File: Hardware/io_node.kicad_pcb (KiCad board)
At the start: 2 copper layers, 60 x 90 mm, 135 parts, among them J1 Conn_01x09, J10 Conn_01x04, J2 Conn_01x09, J3 Conn_01x09, J4 Conn_01x05, J5 USB_B_Micro, J6 Conn_01x05, J7 Conn_01x05, J8 Conn_01x02, J9 Conn_01x04, Q1 2N7002, Q2 2N7002, Q3 2N7002, Q4 2N7002, Q5 2N7002, Q6 2N7002, Q7 2N7002, Q8 2N7002, U1 STM32F103RBT6, U10 EL357N-G, U11 EL357N-G, U12 EL357N-G, U13 EL357N-G, U14 EL357N-G, U15 USBLC6-2SC6, U2 AMS1117-5.0, U3 AMS1117-3.3, U4 SP3485EN, U5 TLV274CPWR, U6 TLV274CPWR, U7 EL357N-G, U8 EL357N-G, U9 EL357N-G, Y1 8 MHz

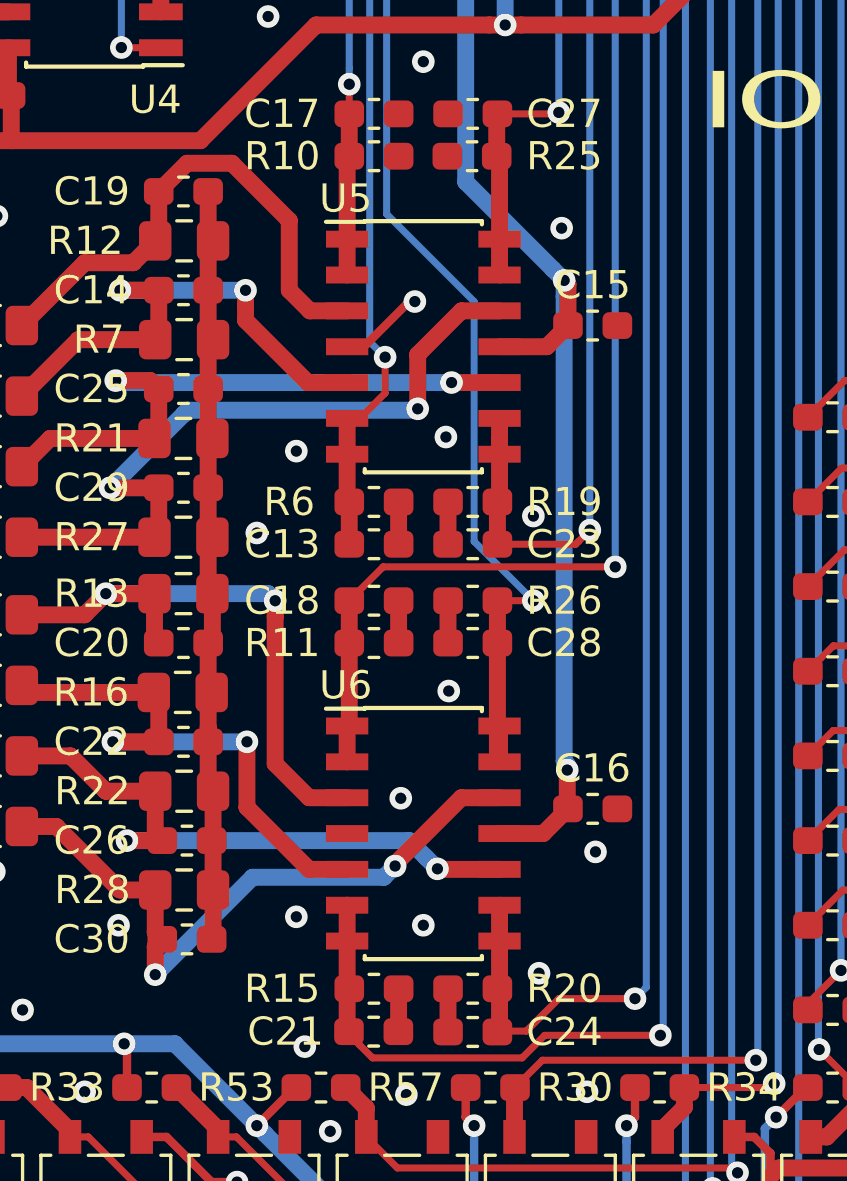
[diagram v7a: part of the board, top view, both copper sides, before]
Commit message: OP-AMP power was incorrect
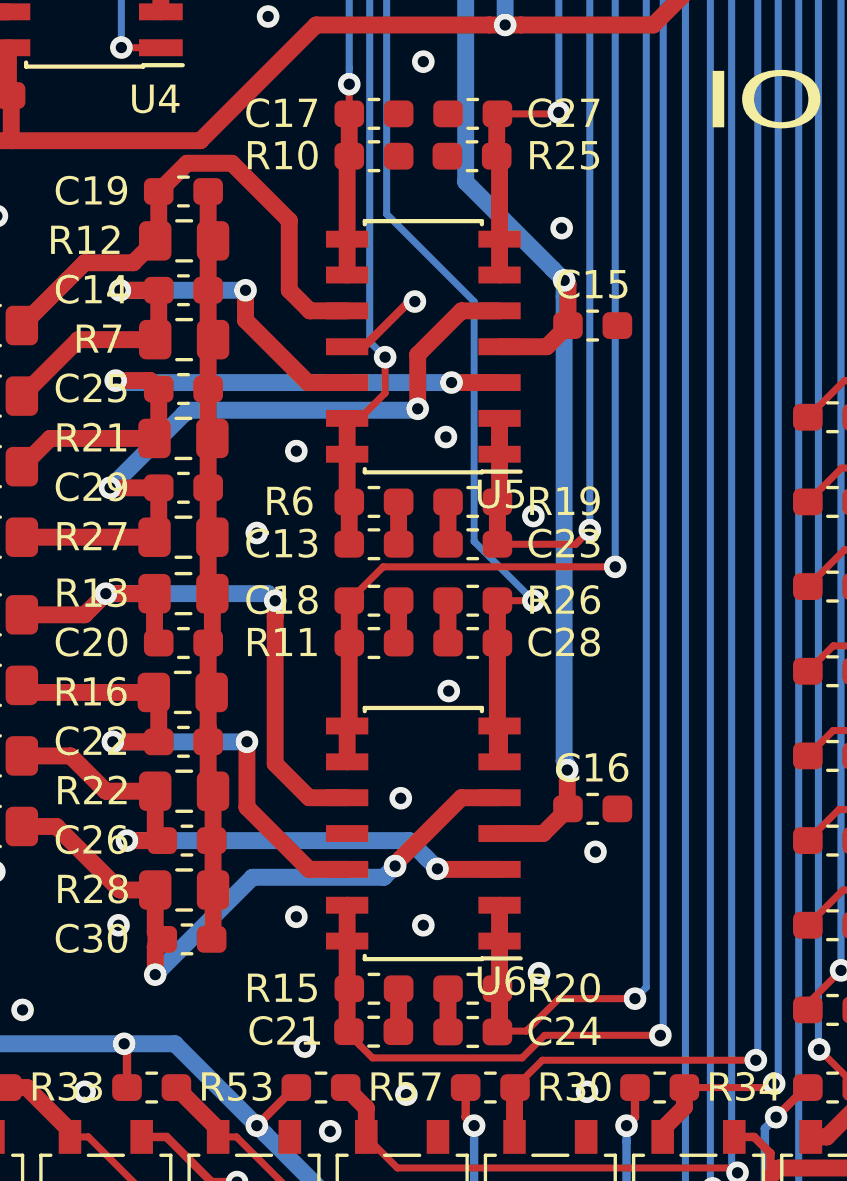
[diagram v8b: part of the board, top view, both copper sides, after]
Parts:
- U5, U6: value TLV274CPWR -> LM324DT
- turned U5 to 180 degrees
- turned U6 to 180 degrees
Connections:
- U5 pad 1: /ADC_IN0 -> /ADC_IN5
- U5 pad 10: Net-(C25-Pad1) -> Net-(C19-Pad1)
- U5 pad 11: +3.3VA -> GND
- U5 pad 12: Net-(C29-Pad1) -> Net-(C14-Pad1)
- U5 pad 13: /ADC_IN6 -> /ADC_IN1
- U5 pad 14: /ADC_IN6 -> /ADC_IN1
- U5 pad 2: /ADC_IN0 -> /ADC_IN5
- U5 pad 3: Net-(C19-Pad1) -> Net-(C25-Pad1)
- U5 pad 4: GND -> +3.3VA
- U5 pad 5: Net-(C14-Pad1) -> Net-(C29-Pad1)
- U5 pad 6: /ADC_IN1 -> /ADC_IN6
- U5 pad 7: /ADC_IN1 -> /ADC_IN6
- U5 pad 8: /ADC_IN5 -> /ADC_IN0
- U5 pad 9: /ADC_IN5 -> /ADC_IN0
- U6 pad 1: /ADC_IN7 -> /ADC_IN9
- U6 pad 10: Net-(C26-Pad1) -> Net-(C20-Pad1)
- U6 pad 11: +3.3VA -> GND
- U6 pad 12: Net-(C30-Pad1) -> Net-(C22-Pad1)
- U6 pad 13: /ADC_IN10 -> /ADC_IN8
- U6 pad 14: /ADC_IN10 -> /ADC_IN8
- U6 pad 2: /ADC_IN7 -> /ADC_IN9
- U6 pad 3: Net-(C20-Pad1) -> Net-(C26-Pad1)
- U6 pad 4: GND -> +3.3VA
- U6 pad 5: Net-(C22-Pad1) -> Net-(C30-Pad1)
- U6 pad 6: /ADC_IN8 -> /ADC_IN10
- U6 pad 7: /ADC_IN8 -> /ADC_IN10
- U6 pad 8: /ADC_IN9 -> /ADC_IN7
- U6 pad 9: /ADC_IN9 -> /ADC_IN7
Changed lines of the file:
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@@
   )
   (module Package_SO:SOIC-14_3.9x8.7mm_P1.27mm (layer F.Cu)
-    (at 69 59)
+    (at 69 59 180)
     (descr "14-Lead Plastic Small Outline (SL) - Narrow, 3.90 mm Body [SOIC] (see Microchip Packaging Specification 00000049BS.pdf)")
     (tags "SOIC 1.27")
     (attr smd)
-    (fp_text reference U5 (at -2.75 -5.25) (layer F.SilkS)
-      (effects (font (size 1 1) (thickness 0.15)))
-    )
-    (fp_text value TLV274CPWR (at 0 5.375) (layer F.Fab)
-      (effects (font (size 1 1) (thickness 0.15)))
-    )
-    (fp_text user %R (at 0 0) (layer F.Fab)
+    (fp_text reference U5 (at -2.75 -5.25 180) (layer F.SilkS)
+      (effects (font (size 1 1) (thickness 0.15)))
+    )
+    (fp_text value LM324DT (at 0 5.375 180) (layer F.Fab)
+      (effects (font (size 1 1) (thickness 0.15)))
+    )
+    (fp_text user %R (at 0 0 180) (layer F.Fab)
       (effects (font (size 0.9 0.9) (thickness 0.135)))
     )
@@
     (fp_line (start -2.075 4.45) (end 2.075 4.45) (layer F.SilkS) (width 0.15))
     (fp_line (start -2.075 -4.425) (end -3.45 -4.425) (layer F.SilkS) (width 0.15))
-    (pad 1 smd rect (at -2.7 -3.81) (size 1.5 0.6) (layers F.Cu F.Paste F.Mask)
+    (pad 1 smd rect (at -2.7 -3.81 180) (size 1.5 0.6) (layers F.Cu F.Paste F.Mask)
+      (net 26 /ADC_IN5))
+    (pad 2 smd rect (at -2.7 -2.54 180) (size 1.5 0.6) (layers F.Cu F.Paste F.Mask)
+      (net 26 /ADC_IN5))
+    (pad 3 smd rect (at -2.7 -1.27 180) (size 1.5 0.6) (layers F.Cu F.Paste F.Mask)
+      (net 35 "Net-(C25-Pad1)"))
+    (pad 4 smd rect (at -2.7 0 180) (size 1.5 0.6) (layers F.Cu F.Paste F.Mask)
+      (net 14 +3.3VA))
+    (pad 5 smd rect (at -2.7 1.27 180) (size 1.5 0.6) (layers F.Cu F.Paste F.Mask)
+      (net 37 "Net-(C29-Pad1)"))
+    (pad 6 smd rect (at -2.7 2.54 180) (size 1.5 0.6) (layers F.Cu F.Paste F.Mask)
+      (net 27 /ADC_IN6))
+    (pad 7 smd rect (at -2.7 3.81 180) (size 1.5 0.6) (layers F.Cu F.Paste F.Mask)
+      (net 27 /ADC_IN6))
+    (pad 8 smd rect (at 2.7 3.81 180) (size 1.5 0.6) (layers F.Cu F.Paste F.Mask)
       (net 24 /ADC_IN0))
-    (pad 2 smd rect (at -2.7 -2.54) (size 1.5 0.6) (layers F.Cu F.Paste F.Mask)
+    (pad 9 smd rect (at 2.7 2.54 180) (size 1.5 0.6) (layers F.Cu F.Paste F.Mask)
       (net 24 /ADC_IN0))
-    (pad 3 smd rect (at -2.7 -1.27) (size 1.5 0.6) (layers F.Cu F.Paste F.Mask)
+    (pad 10 smd rect (at 2.7 1.27 180) (size 1.5 0.6) (layers F.Cu F.Paste F.Mask)
       (net 32 "Net-(C19-Pad1)"))
-    (pad 4 smd rect (at -2.7 0) (size 1.5 0.6) (layers F.Cu F.Paste F.Mask)
-      (net 1 GND))
-    (pad 5 smd rect (at -2.7 1.27) (size 1.5 0.6) (layers F.Cu F.Paste F.Mask)
+    (pad 11 smd rect (at 2.7 0 180) (size 1.5 0.6) (layers F.Cu F.Paste F.Mask)
+      (net 1 GND))
+    (pad 12 smd rect (at 2.7 -1.27 180) (size 1.5 0.6) (layers F.Cu F.Paste F.Mask)
       (net 31 "Net-(C14-Pad1)"))
-    (pad 6 smd rect (at -2.7 2.54) (size 1.5 0.6) (layers F.Cu F.Paste F.Mask)
+    (pad 13 smd rect (at 2.7 -2.54 180) (size 1.5 0.6) (layers F.Cu F.Paste F.Mask)
       (net 25 /ADC_IN1))
-    (pad 7 smd rect (at -2.7 3.81) (size 1.5 0.6) (layers F.Cu F.Paste F.Mask)
+    (pad 14 smd rect (at 2.7 -3.81 180) (size 1.5 0.6) (layers F.Cu F.Paste F.Mask)
       (net 25 /ADC_IN1))
-    (pad 8 smd rect (at 2.7 3.81) (size 1.5 0.6) (layers F.Cu F.Paste F.Mask)
-      (net 26 /ADC_IN5))
-    (pad 9 smd rect (at 2.7 2.54) (size 1.5 0.6) (layers F.Cu F.Paste F.Mask)
-      (net 26 /ADC_IN5))
-    (pad 10 smd rect (at 2.7 1.27) (size 1.5 0.6) (layers F.Cu F.Paste F.Mask)
-      (net 35 "Net-(C25-Pad1)"))
-    (pad 11 smd rect (at 2.7 0) (size 1.5 0.6) (layers F.Cu F.Paste F.Mask)
-      (net 14 +3.3VA))
-    (pad 12 smd rect (at 2.7 -1.27) (size 1.5 0.6) (layers F.Cu F.Paste F.Mask)
-      (net 37 "Net-(C29-Pad1)"))
-    (pad 13 smd rect (at 2.7 -2.54) (size 1.5 0.6) (layers F.Cu F.Paste F.Mask)
-      (net 27 /ADC_IN6))
-    (pad 14 smd rect (at 2.7 -3.81) (size 1.5 0.6) (layers F.Cu F.Paste F.Mask)
-      (net 27 /ADC_IN6))
     (model ${KISYS3DMOD}/Package_SO.3dshapes/SOIC-14_3.9x8.7mm_P1.27mm.wrl
       (at (xyz 0 0 0))
@@
   )
   (module Package_SO:SOIC-14_3.9x8.7mm_P1.27mm (layer F.Cu)
-    (at 69 76.25)
+    (at 69 76.25 180)
     (descr "14-Lead Plastic Small Outline (SL) - Narrow, 3.90 mm Body [SOIC] (see Microchip Packaging Specification 00000049BS.pdf)")
     (tags "SOIC 1.27")
     (attr smd)
-    (fp_text reference U6 (at -2.75 -5.25) (layer F.SilkS)
-      (effects (font (size 1 1) (thickness 0.15)))
-    )
-    (fp_text value TLV274CPWR (at 0 5.375) (layer F.Fab)
-      (effects (font (size 1 1) (thickness 0.15)))
-    )
-    (fp_text user %R (at 0 0) (layer F.Fab)
+    (fp_text reference U6 (at -2.75 -5.25 180) (layer F.SilkS)
+      (effects (font (size 1 1) (thickness 0.15)))
+    )
+    (fp_text value LM324DT (at 0 5.375 180) (layer F.Fab)
+      (effects (font (size 1 1) (thickness 0.15)))
+    )
+    (fp_text user %R (at 0 0 180) (layer F.Fab)
       (effects (font (size 0.9 0.9) (thickness 0.135)))
     )
@@
     (fp_line (start -2.075 4.45) (end 2.075 4.45) (layer F.SilkS) (width 0.15))
     (fp_line (start -2.075 -4.425) (end -3.45 -4.425) (layer F.SilkS) (width 0.15))
-    (pad 1 smd rect (at -2.7 -3.81) (size 1.5 0.6) (layers F.Cu F.Paste F.Mask)
+    (pad 1 smd rect (at -2.7 -3.81 180) (size 1.5 0.6) (layers F.Cu F.Paste F.Mask)
+      (net 30 /ADC_IN9))
+    (pad 2 smd rect (at -2.7 -2.54 180) (size 1.5 0.6) (layers F.Cu F.Paste F.Mask)
+      (net 30 /ADC_IN9))
+    (pad 3 smd rect (at -2.7 -1.27 180) (size 1.5 0.6) (layers F.Cu F.Paste F.Mask)
+      (net 36 "Net-(C26-Pad1)"))
+    (pad 4 smd rect (at -2.7 0 180) (size 1.5 0.6) (layers F.Cu F.Paste F.Mask)
+      (net 14 +3.3VA))
+    (pad 5 smd rect (at -2.7 1.27 180) (size 1.5 0.6) (layers F.Cu F.Paste F.Mask)
+      (net 38 "Net-(C30-Pad1)"))
+    (pad 6 smd rect (at -2.7 2.54 180) (size 1.5 0.6) (layers F.Cu F.Paste F.Mask)
+      (net 75 /ADC_IN10))
+    (pad 7 smd rect (at -2.7 3.81 180) (size 1.5 0.6) (layers F.Cu F.Paste F.Mask)
+      (net 75 /ADC_IN10))
+    (pad 8 smd rect (at 2.7 3.81 180) (size 1.5 0.6) (layers F.Cu F.Paste F.Mask)
       (net 28 /ADC_IN7))
-    (pad 2 smd rect (at -2.7 -2.54) (size 1.5 0.6) (layers F.Cu F.Paste F.Mask)
+    (pad 9 smd rect (at 2.7 2.54 180) (size 1.5 0.6) (layers F.Cu F.Paste F.Mask)
       (net 28 /ADC_IN7))
-    (pad 3 smd rect (at -2.7 -1.27) (size 1.5 0.6) (layers F.Cu F.Paste F.Mask)
+    (pad 10 smd rect (at 2.7 1.27 180) (size 1.5 0.6) (layers F.Cu F.Paste F.Mask)
       (net 33 "Net-(C20-Pad1)"))
-    (pad 4 smd rect (at -2.7 0) (size 1.5 0.6) (layers F.Cu F.Paste F.Mask)
-      (net 1 GND))
-    (pad 5 smd rect (at -2.7 1.27) (size 1.5 0.6) (layers F.Cu F.Paste F.Mask)
+    (pad 11 smd rect (at 2.7 0 180) (size 1.5 0.6) (layers F.Cu F.Paste F.Mask)
+      (net 1 GND))
+    (pad 12 smd rect (at 2.7 -1.27 180) (size 1.5 0.6) (layers F.Cu F.Paste F.Mask)
       (net 34 "Net-(C22-Pad1)"))
-    (pad 6 smd rect (at -2.7 2.54) (size 1.5 0.6) (layers F.Cu F.Paste F.Mask)
+    (pad 13 smd rect (at 2.7 -2.54 180) (size 1.5 0.6) (layers F.Cu F.Paste F.Mask)
       (net 29 /ADC_IN8))
-    (pad 7 smd rect (at -2.7 3.81) (size 1.5 0.6) (layers F.Cu F.Paste F.Mask)
+    (pad 14 smd rect (at 2.7 -3.81 180) (size 1.5 0.6) (layers F.Cu F.Paste F.Mask)
       (net 29 /ADC_IN8))
-    (pad 8 smd rect (at 2.7 3.81) (size 1.5 0.6) (layers F.Cu F.Paste F.Mask)
-      (net 30 /ADC_IN9))
-    (pad 9 smd rect (at 2.7 2.54) (size 1.5 0.6) (layers F.Cu F.Paste F.Mask)
-      (net 30 /ADC_IN9))
-    (pad 10 smd rect (at 2.7 1.27) (size 1.5 0.6) (layers F.Cu F.Paste F.Mask)
-      (net 36 "Net-(C26-Pad1)"))
-    (pad 11 smd rect (at 2.7 0) (size 1.5 0.6) (layers F.Cu F.Paste F.Mask)
-      (net 14 +3.3VA))
-    (pad 12 smd rect (at 2.7 -1.27) (size 1.5 0.6) (layers F.Cu F.Paste F.Mask)
-      (net 38 "Net-(C30-Pad1)"))
-    (pad 13 smd rect (at 2.7 -2.54) (size 1.5 0.6) (layers F.Cu F.Paste F.Mask)
-      (net 75 /ADC_IN10))
-    (pad 14 smd rect (at 2.7 -3.81) (size 1.5 0.6) (layers F.Cu F.Paste F.Mask)
-      (net 75 /ADC_IN10))
     (model ${KISYS3DMOD}/Package_SO.3dshapes/SOIC-14_3.9x8.7mm_P1.27mm.wrl
       (at (xyz 0 0 0))
